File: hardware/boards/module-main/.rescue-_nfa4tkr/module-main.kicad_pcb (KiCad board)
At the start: 4 copper layers, 48.5 x 108.5 mm, 177 parts, among them J1 2x8 2.54mm shrouded box heade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, J2 2x10 2.54mm pin header, J3 Neutrik NE8FAV, J4 JST B2B-XH-A, Q1 PSMN2R0-30YLE, SW1 NKK M2011SD4G01, U1 LT3042EMSE, U10 OPA2197, U11 OPA2197, U12 OPA2197, U13 ADP7118AUJZ-5.0, U14 RPA20-2412SAW, U15 74AHCT14, U2 LT1641-1IS8, U3 DAC8568ICPW, U4 74AHCT125, U5 OPA2197, U6 INA828IDR, U7 OPA2197, U8 OPA2197IDR, U9 OPA2197

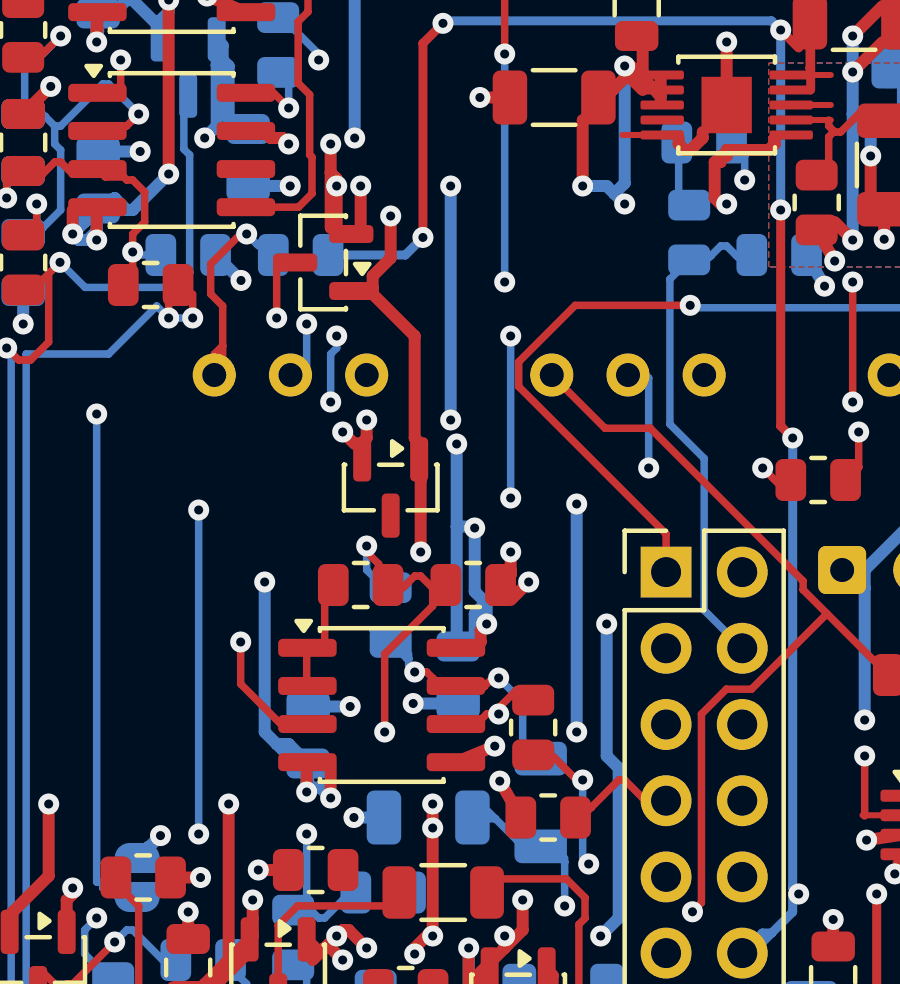
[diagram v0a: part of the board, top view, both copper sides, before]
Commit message: module-main: the moat's keep-out opened round U-DAC (it straddles the moat) and wider round the star's tie; routing state 23 left
Co-Authored-By: Claude Opus 5.5 <noreply@anthropic.com>
Claude-Session: https://claude.ai/code/session_01LmB4muFXnoLprWX4JzuJ5A
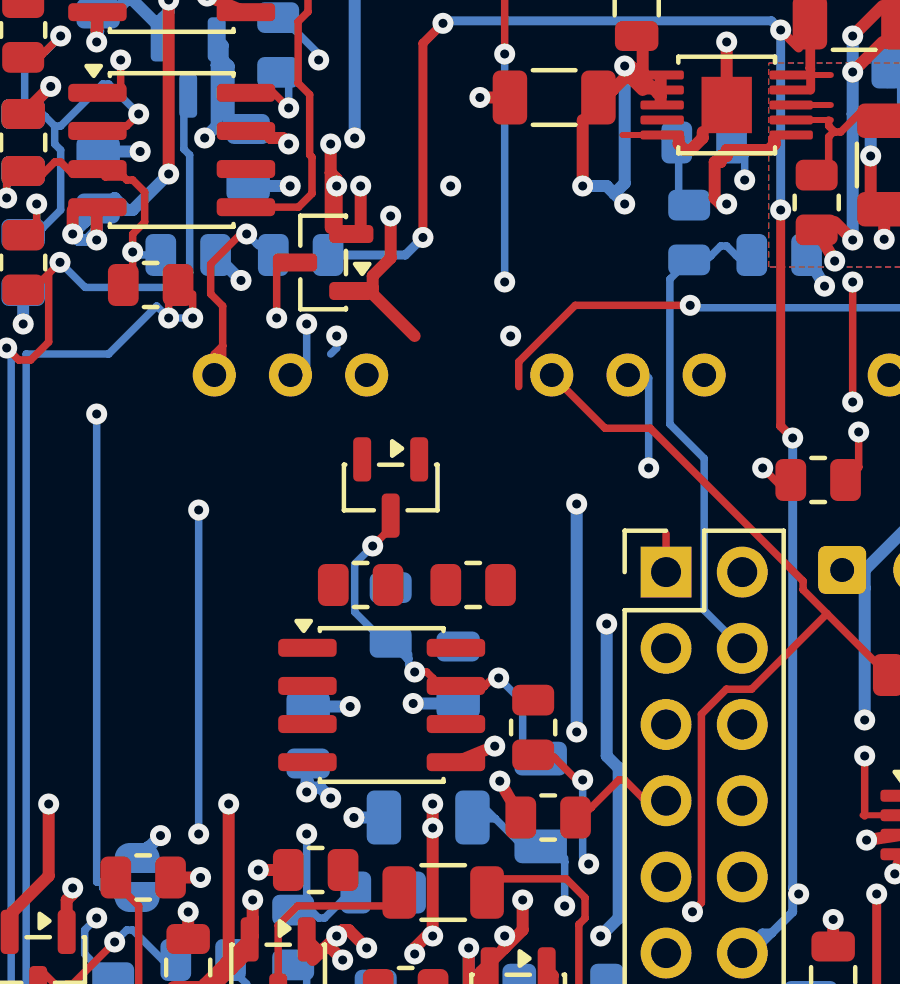
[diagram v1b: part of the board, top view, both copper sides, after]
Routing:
- net MODULE_ANALOG_POS12: track 343.8 -> 297.9 mm, vias 41 -> 35
- net MODULE_ANALOG_NEG12: track 302.3 -> 267.3 mm, vias 48 -> 44
- net /dac8568/CLR: track 166.5 -> 145.2 mm, vias 12 -> 11
- net /breath-output-stage/SUM_NODE: track 18.7 -> 0.00 mm, vias 3 -> 0
- net /mod-channels/MINUS_3: track 149.1 -> 133.1 mm, vias 8 -> 7
- net /GAIN_WIPER: track 17.2 -> 1.68 mm, vias 1 -> 0
- net /BREATH_SHAPED: track 36.8 -> 29.9 mm
- net /breath-output-stage/BUF_OUT: track 3.97 -> 0.00 mm
- net /breath-output-stage/BREATH_OUT: track 9.49 -> 13.4 mm, vias 2 -> 3
